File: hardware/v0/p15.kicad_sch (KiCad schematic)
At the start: 99 parts, among them J2 USB4105-GF-A, SW1 SW_Push, U1 ATmega32U4-AU, U2 TPD4EUSB30, Y1 16MHz

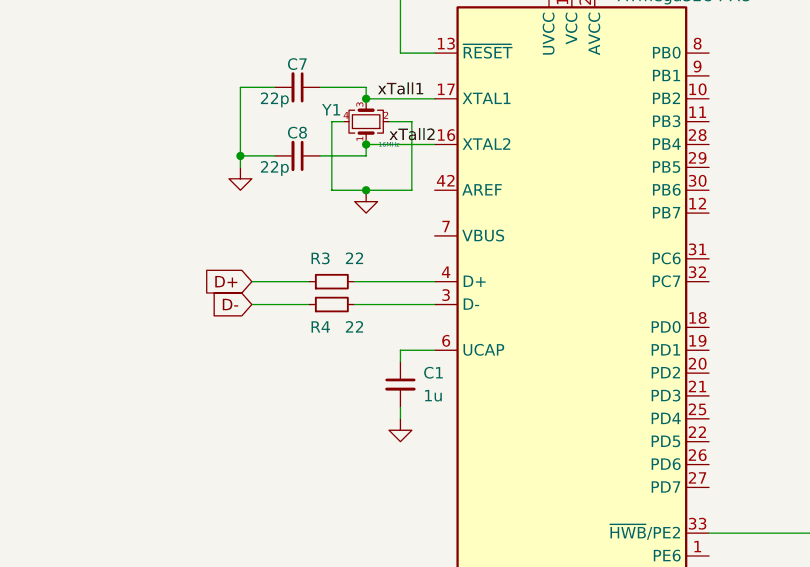
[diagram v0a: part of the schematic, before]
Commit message: routed crytal
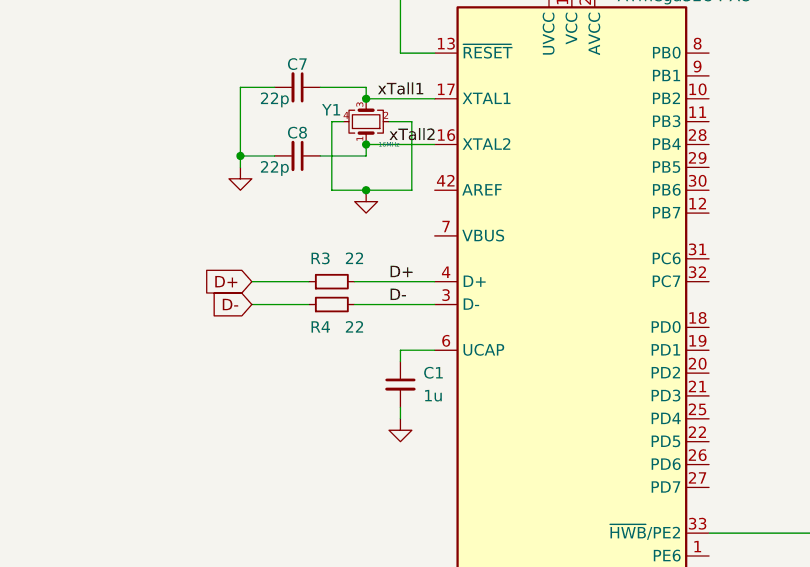
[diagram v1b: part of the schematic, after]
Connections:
- net D+: now also R3.2, U1.4 (D+)
- net D-: now also R4.2, U1.3 (D-)
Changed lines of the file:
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@@
     (effects (font (size 4 4) (thickness 0.8) bold italic) (justify left bottom))
+  )
+  (label "D-" (at 341.63 165.1 0)
+    (effects (font (size 1.27 1.27)) (justify left bottom))
   )
   (label "NRST" (at 342.9 130.81 0)
@@
     (effects (font (size 1.27 1.27)) (justify left bottom))
   )
+  (label "D+" (at 341.63 162.56 0)
+    (effects (font (size 1.27 1.27)) (justify left bottom))
+  )

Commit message: more routing
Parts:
- added C? (x2): 100n, Capacitor_SMD:C_0805_2012Metric_Pad1.18x1.45mm_HandSolder, symbol Device:C_Small
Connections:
- net +5V: now also U1.42 (AREF), U1.7 (VBUS), C?.1, C?.1
- net GND: now also C?.2, C?.2
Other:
- moved on the sheet: C2, C3, C4, C5, C6

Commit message: more routing
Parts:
- gave numbers to parts that had none: 2
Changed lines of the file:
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@@
   (symbol (lib_id "Device:C_Small") (at 382.27 94.615 0) (unit 1)
     (in_bom yes) (on_board yes) (fields_autoplaced)
-    (property "Reference" "C?" (id 0) (at 384.81 93.3512 0)
+    (property "Reference" "C31" (id 0) (at 384.81 93.3512 0)
       (effects (font (size 1.27 1.27)) (justify left))
     )
@@
   (symbol (lib_id "Device:C_Small") (at 391.16 94.615 0) (unit 1)
     (in_bom yes) (on_board yes) (fields_autoplaced)
-    (property "Reference" "C?" (id 0) (at 393.7 93.3512 0)
+    (property "Reference" "C32" (id 0) (at 393.7 93.3512 0)
       (effects (font (size 1.27 1.27)) (justify left))
     )
@@
     )
     (path "/45f1e93a-5fe4-4905-9e61-7663f1a6b11c"
-      (reference "C?") (unit 1) (value "100n") (footprint "Capacitor_SMD:C_0805_2012Metric_Pad1.18x1.45mm_HandSolder")
+      (reference "C31") (unit 1) (value "100n") (footprint "Capacitor_SMD:C_0805_2012Metric_Pad1.18x1.45mm_HandSolder")
     )
     (path "/d95acf0e-0a65-4792-860c-c2632bba2121"
-      (reference "C?") (unit 1) (value "100n") (footprint "Capacitor_SMD:C_0805_2012Metric_Pad1.18x1.45mm_HandSolder")
+      (reference "C32") (unit 1) (value "100n") (footprint "Capacitor_SMD:C_0805_2012Metric_Pad1.18x1.45mm_HandSolder")
     )
     (path "/c425f06b-28e1-4865-9739-17189647c214"
